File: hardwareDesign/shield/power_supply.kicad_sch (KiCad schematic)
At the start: 6 parts, among them J4 10_POS_PIN_HEADER_ALT, Q1 FDMS4435BZ, U8 LD29150DT50R

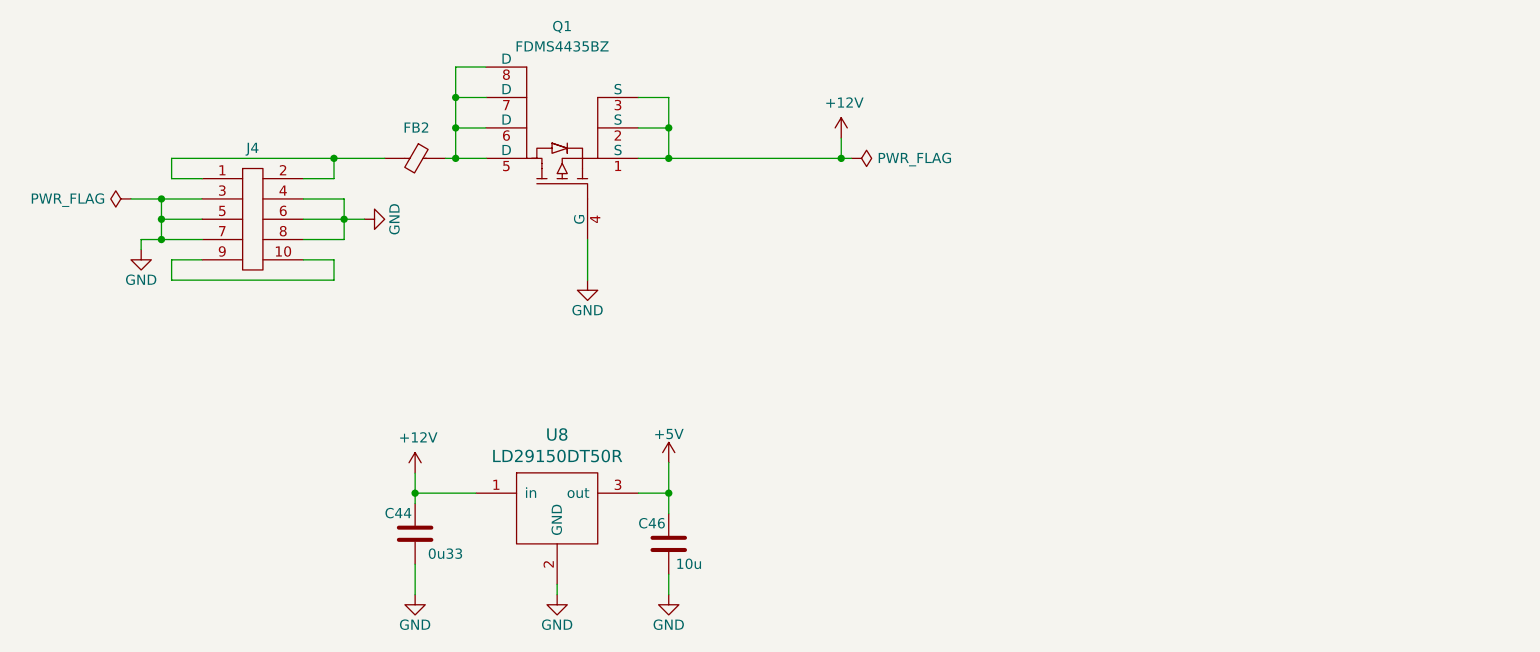
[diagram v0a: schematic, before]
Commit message: Schematic done
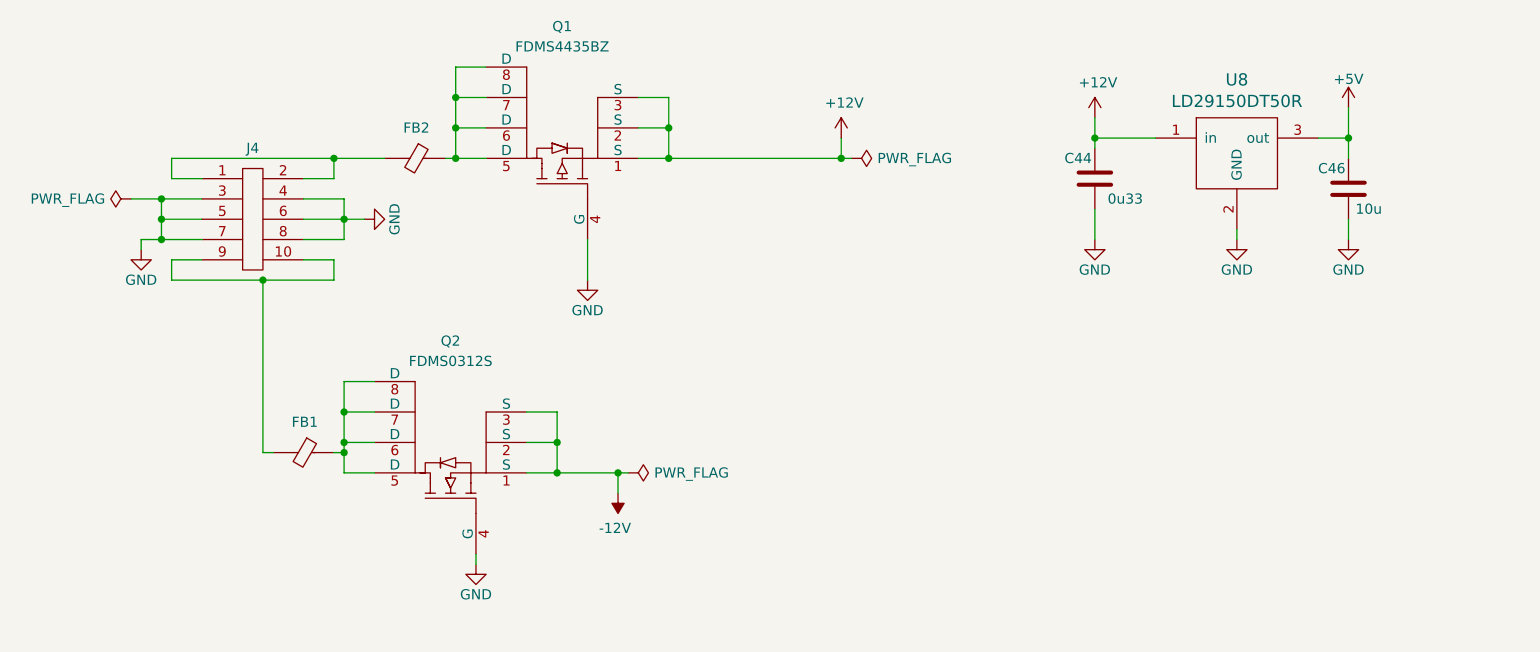
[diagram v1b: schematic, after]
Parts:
- added FB1: FB_HZ0805, inductance_ferrite:FB_HZ0805, symbol inductors:FB_HZ0805
- added Q2: FDMS0312S, transistors:Power-56-8, symbol transistors:FDMS0312S
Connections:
- net GND: now also Q2.4 (G)
- net at J4.10, J4.9: now also FB1.2
- new net: FB1.1, Q2.5 (D), Q2.6 (D), Q2.7 (D), Q2.8 (D)
- new net -12V: Q2.1 (S), Q2.2 (S), Q2.3 (S)
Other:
- moved on the sheet: C44, C46, U8

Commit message: Finished schematic and PCB for jetson Nano Sheild
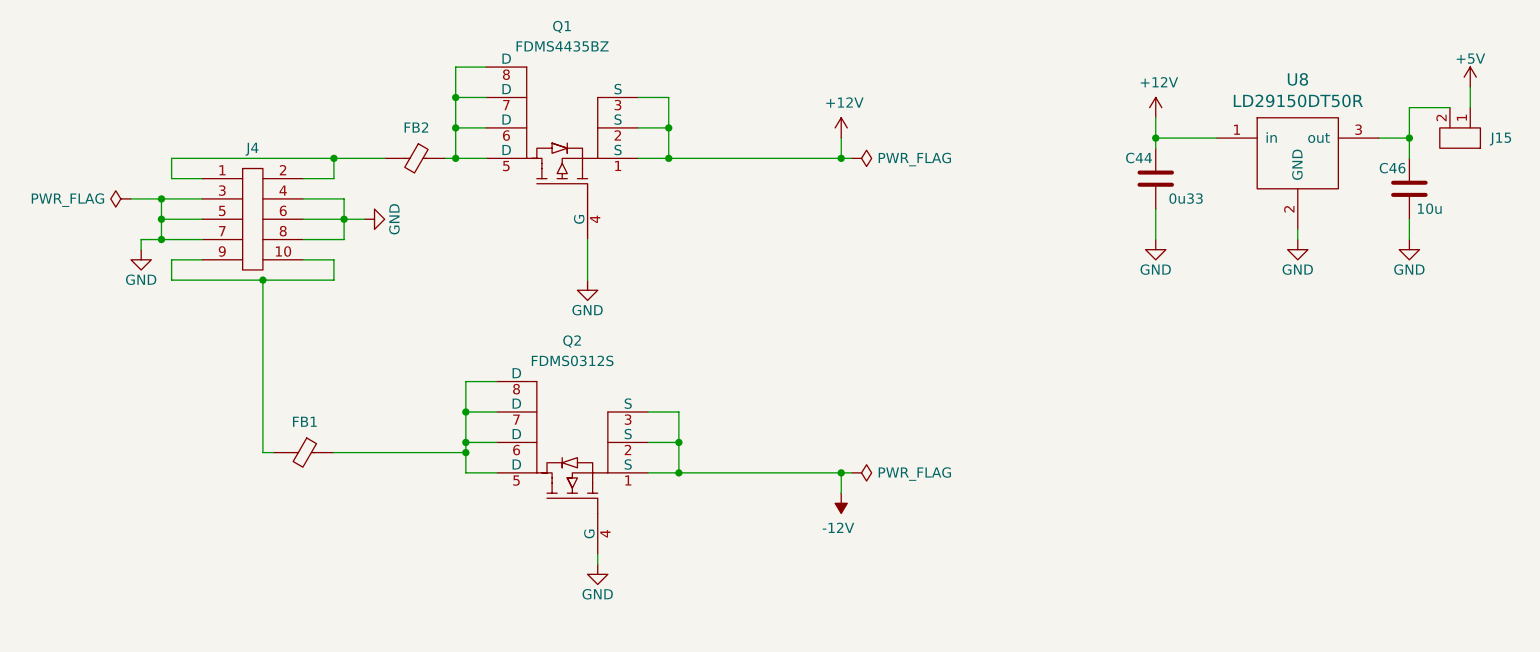
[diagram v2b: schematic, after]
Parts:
- added J15: 2x1_PIN_HEADER, connectors:02x01_2.54_pitch_pin_header, symbol connectors:2x1_PIN_HEADER
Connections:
- net +5V: now also J15.1; no longer C46.1, U8.3 (out)
- new net: C46.1, J15.2, U8.3 (out)
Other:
- moved on the sheet: C44, C46, Q2, U8
